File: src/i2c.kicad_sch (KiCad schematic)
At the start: 0 parts

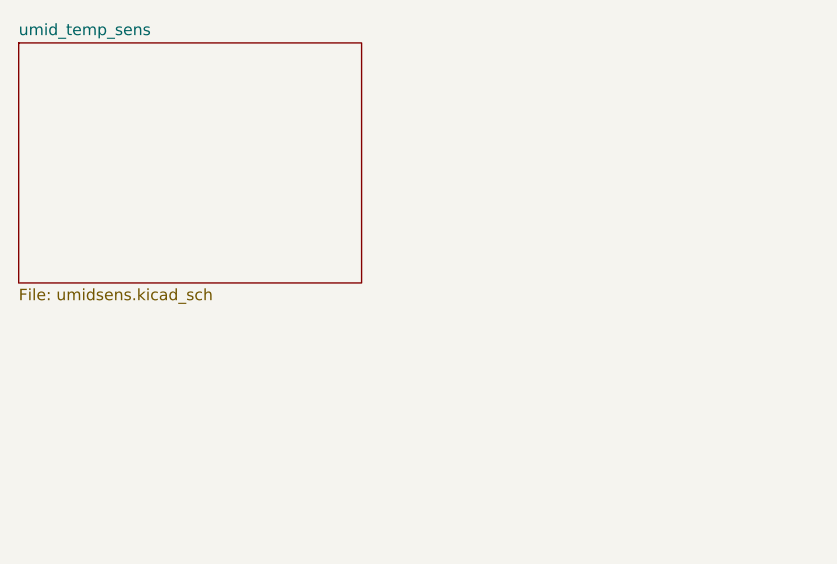
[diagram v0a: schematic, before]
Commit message: fix: Consertando paginação e refact da Tela_OLED
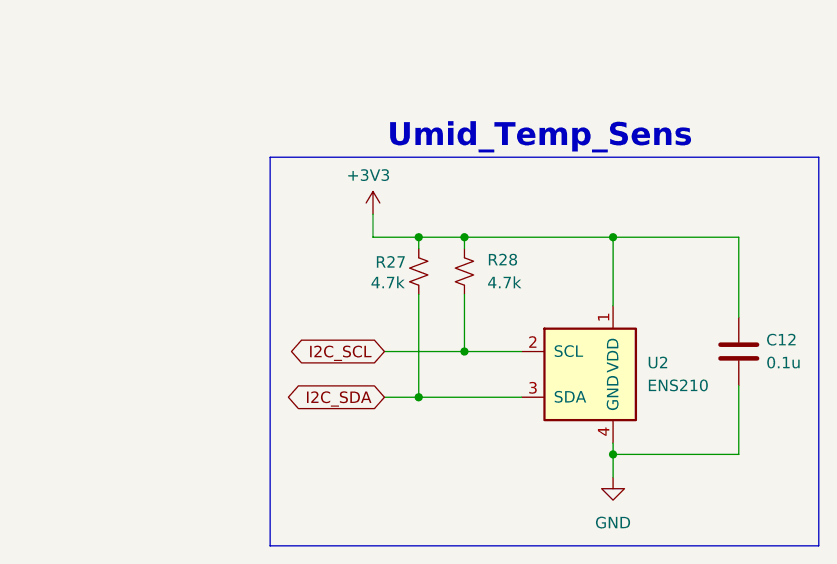
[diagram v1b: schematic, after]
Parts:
- added C12: 0.1u, symbol Device:C
- added R27, R28: 4.7k, symbol Device:R_Small_US
- added U2: ENS210, Package_DFN_QFN:AMS_QFN-4-1EP_2x2mm_P0.95mm_EP0.7x1.6mm, symbol Sensor_Humidity:ENS210
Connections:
- new net +3V3: C12.1, R27.1, R28.1, U2.1 (VDD)
- new net GND: C12.2, U2.4 (GND), U2.5 (GND)
- new net I2C_SCL: R28.2, U2.2 (SCL)
- new net I2C_SDA: R27.2, U2.3 (SDA)
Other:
- removed sheet umid_temp_sens
- note added: "Umid_Temp_Sens"

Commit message: adicionado footprints, falta microfone e display somente
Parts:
- C12: footprint (none) -> Capacitor_SMD:C_0402_1005Metric
- R27, R28: footprint (none) -> Resistor_SMD:R_0402_1005Metric
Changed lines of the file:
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@@
 			)
 		)
-		(property "Footprint" ""
+		(property "Footprint" "Capacitor_SMD:C_0402_1005Metric"
 			(at 166.0652 109.22 0)
 			(effects
@@
 			)
 		)
-		(property "Footprint" ""
+		(property "Footprint" "Resistor_SMD:R_0402_1005Metric"
 			(at 129.54 96.52 0)
 			(effects
@@
 			)
 		)
-		(property "Footprint" ""
+		(property "Footprint" "Resistor_SMD:R_0402_1005Metric"
 			(at 134.62 96.52 0)
 			(effects
